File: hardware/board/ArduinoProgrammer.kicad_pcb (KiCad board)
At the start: 2 copper layers, 25 parts, among them J1 ISP_Programmer, J2 OLED_VCC-GND, J4 CONN_02X16, J5 CONN_01X02, J6 OLED_GND-VCC, SW1 SW_Push, SW2 SW_Push, U1 MIC5219-3.3BM5, U2 ATMEGA328-AU

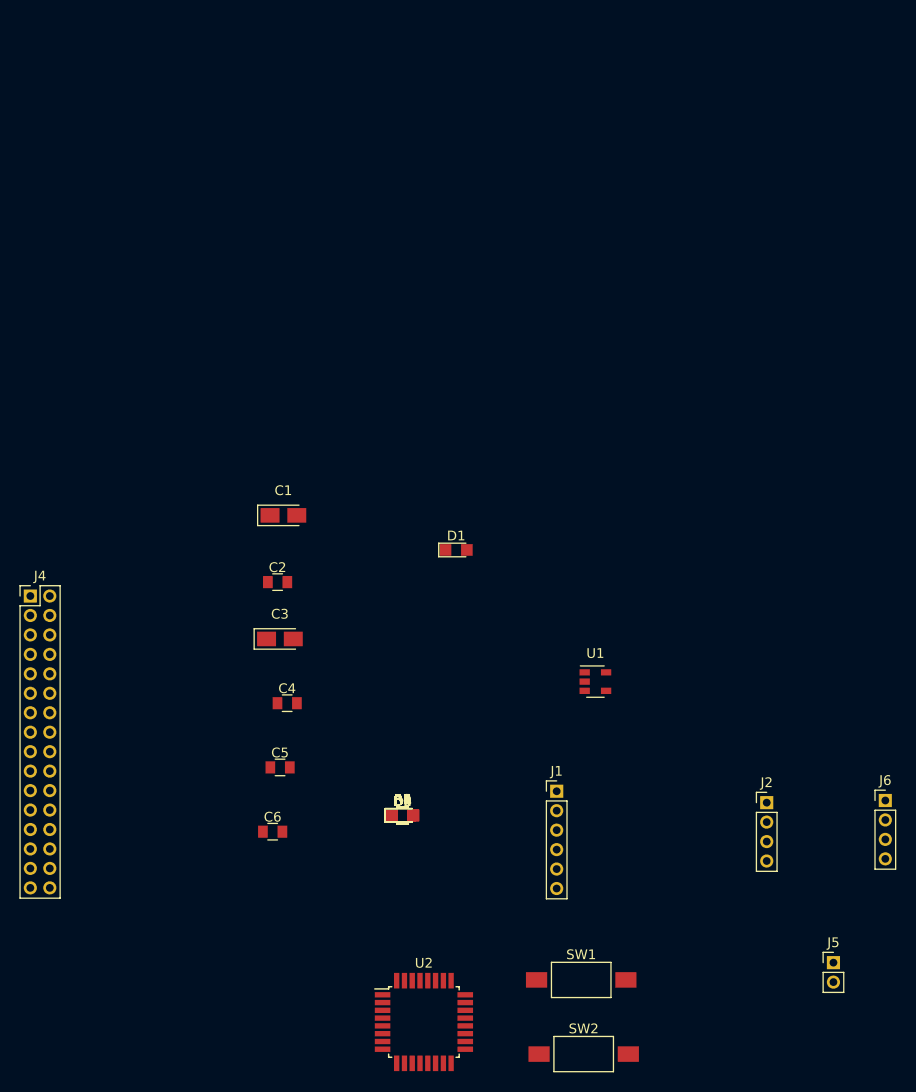
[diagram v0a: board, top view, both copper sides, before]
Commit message: Added pcb circuit with OSx auto-route
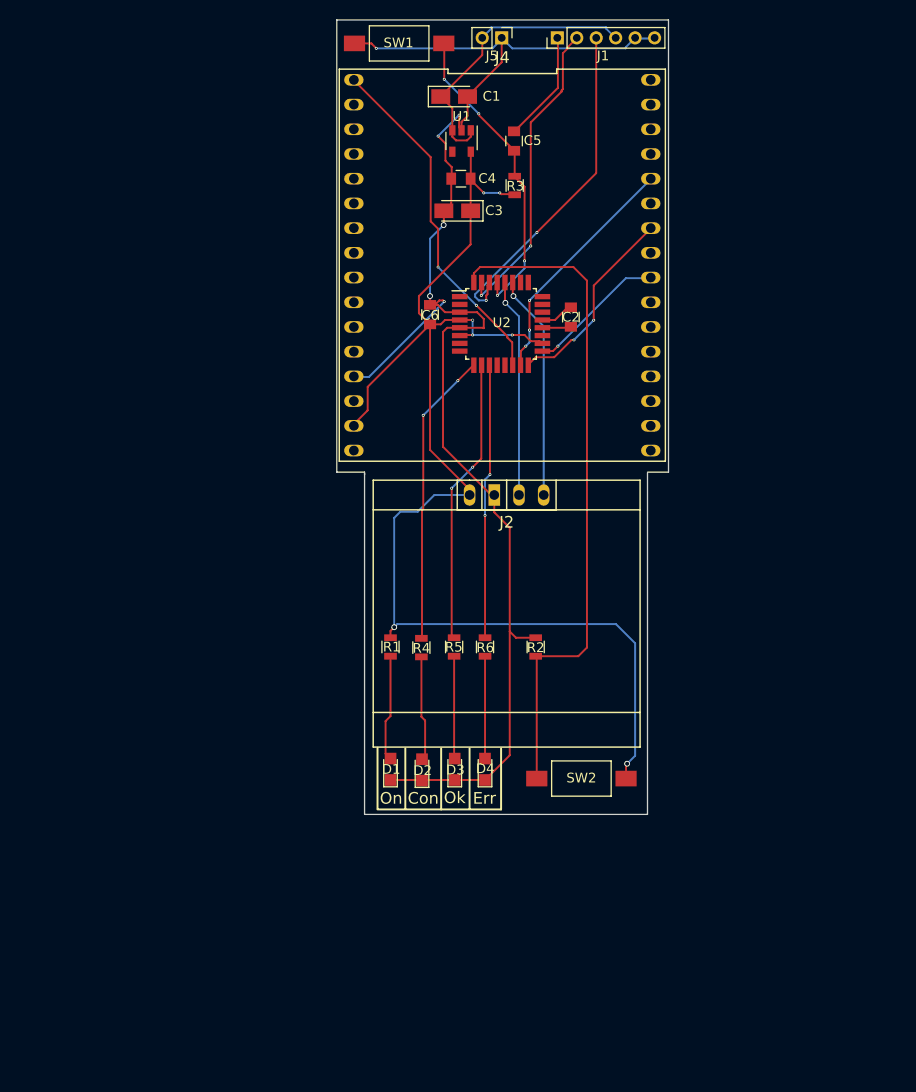
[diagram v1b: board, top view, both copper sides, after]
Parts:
- removed J6: OLED_GND-VCC, Pin_Headers:Pin_Header_Straight_1x04_Pitch2.00mm
- J2: value OLED_VCC-GND -> OLED_VCC_GND; footprint Pin_Headers:Pin_Header_Straight_1x04_Pitch2.00mm -> AtMegaProgrammer:OLED_VCC_GND
- J4: footprint Pin_Headers:Pin_Header_Straight_2x16_Pitch2.00mm -> AtMegaProgrammer:ProgSocket
- moved J5 101.0 mm to (158.7, 25.1), turned to 270 degrees
- moved SW1 98.1 mm to (148.1, 25.7), turned to 180 degrees
- moved J1 77.4 mm to (164.4, 25.1), turned to 90 degrees
- moved U2 72.2 mm to (158.6, 54.5)
- moved C5 68.7 mm to (160.0, 35.7), turned to 270 degrees
- moved R3 65.8 mm to (160.0, 40.3), turned to 90 degrees
- moved J4 59.2 mm to (158.8, 48.5), turned to 270 degrees
- moved U1 57.2 mm to (154.6, 35.7), turned to 270 degrees
- moved C4 56.8 mm to (154.5, 39.6), turned to 180 degrees
- moved C6 55.6 mm to (151.3, 53.5), turned to 90 degrees
- moved C3 47.6 mm to (154.1, 42.9), turned to 180 degrees
- moved C1 46.5 mm to (153.8, 31.1)
- moved J2 41.6 mm to (159.2, 71.8)
- moved C2 40.6 mm to (165.8, 53.8), turned to 90 degrees
- moved SW2 28.3 mm to (166.9, 101.2)
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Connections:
- C1 pad 1: GND -> +5V
- J1 pad 4: GND -> +5V
- J2 pad 1: GND -> VCC
- J2 pad 2: VCC -> GND
- J5 pad 2: GND -> +5V
- U1 pad 1: GND -> +5V
- U1 pad 3: GND -> +5V
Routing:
- net GND: track 0.00 -> 160.0 mm, vias 0 -> 6
- net VCC: track 0.00 -> 135.1 mm, vias 0 -> 7
- net INT: track 0.00 -> 69.4 mm
- net P_RST: track 0.00 -> 36.1 mm, vias 0 -> 2
- net TXO: track 0.00 -> 35.1 mm, vias 0 -> 2
- net Net-(C5-Pad2): track 0.00 -> 32.0 mm, vias 0 -> 4
- net RXO: track 0.00 -> 31.9 mm, vias 0 -> 2
- net D5: track 0.00 -> 30.6 mm, vias 0 -> 2
- net +5V: track 0.00 -> 30.3 mm
- net D6: track 0.00 -> 29.5 mm, vias 0 -> 2
- net D7: track 0.00 -> 28.4 mm, vias 0 -> 2
- net P_MOSI: track 0.00 -> 24.7 mm, vias 0 -> 3
- net SDA: track 0.00 -> 23.2 mm, vias 0 -> 1
- net SCL: track 0.00 -> 22.4 mm, vias 0 -> 1
- net P_MISO: track 0.00 -> 20.6 mm, vias 0 -> 2
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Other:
- board outline added: 34.1 x 81.7 mm
- net class Default: trace_width 0.25 -> 0.2; via_dia 0.6 -> 0.3; via_drill 0.4 -> 0.2
- rule pad_to_mask_clearance: 0.2 -> 0
- rule trace_min: 0.2 -> 0.15
- rule via_min_drill: 0.3 -> 0.13
- rule via_min_size: 0.4 -> 0.26
- board text added: "Con"
- board text added: "Err"
- board text added: "Ok"
- board text added: "On"
